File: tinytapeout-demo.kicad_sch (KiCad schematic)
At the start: 137 parts, among them J1 Conn_01x06, J12 613012243121, J13 613012243121, J14 613012243121, J15 USB4500-03-0-A_REVA, J16 2x20_P2.54mm_Pinheader, J17 Conn_01x03, J18 2x20_P2.54mm_Pinheader, J19 Conn_01x02, J2 Conn_01x04, J3 613012243121, J4 TT04_BREAKOUT_REVB, J5 613012243121, J6 613012243121, J7 Conn_01x02, J8 Conn_01x03, J9 Conn_01x24, SW1 434121025816, SW2 434121025816, SW3 434121025816, SW4 418121270808, U1 157112V12700, U2 TLV1117LV33, U3 AP2112K-1.8, U4 74CBTLV3257, U7 W25Q32JVSS, X1 20MHz

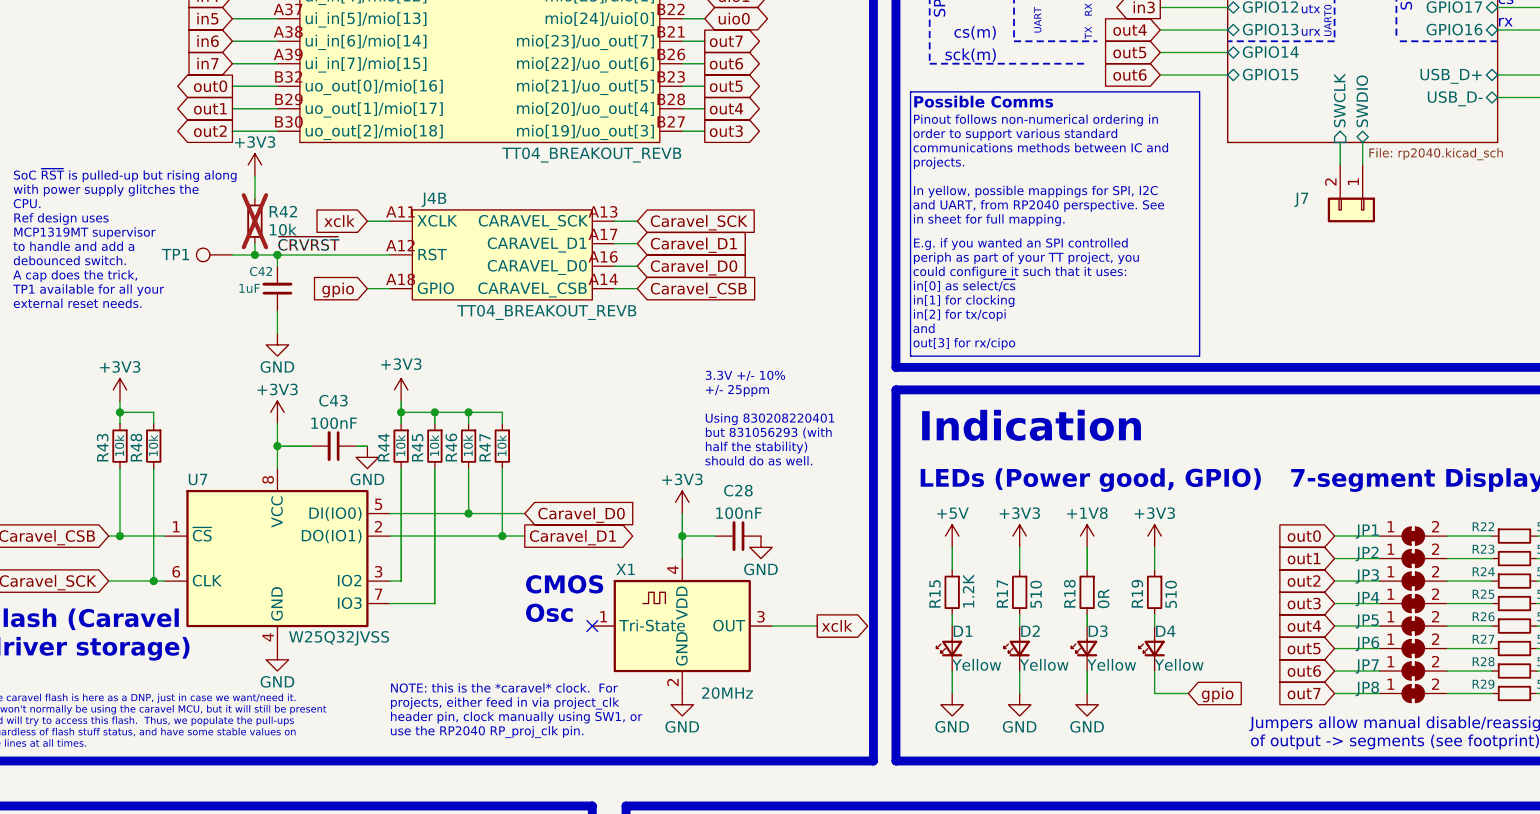
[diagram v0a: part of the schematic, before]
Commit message: Modified silk and BOM for TT04 run
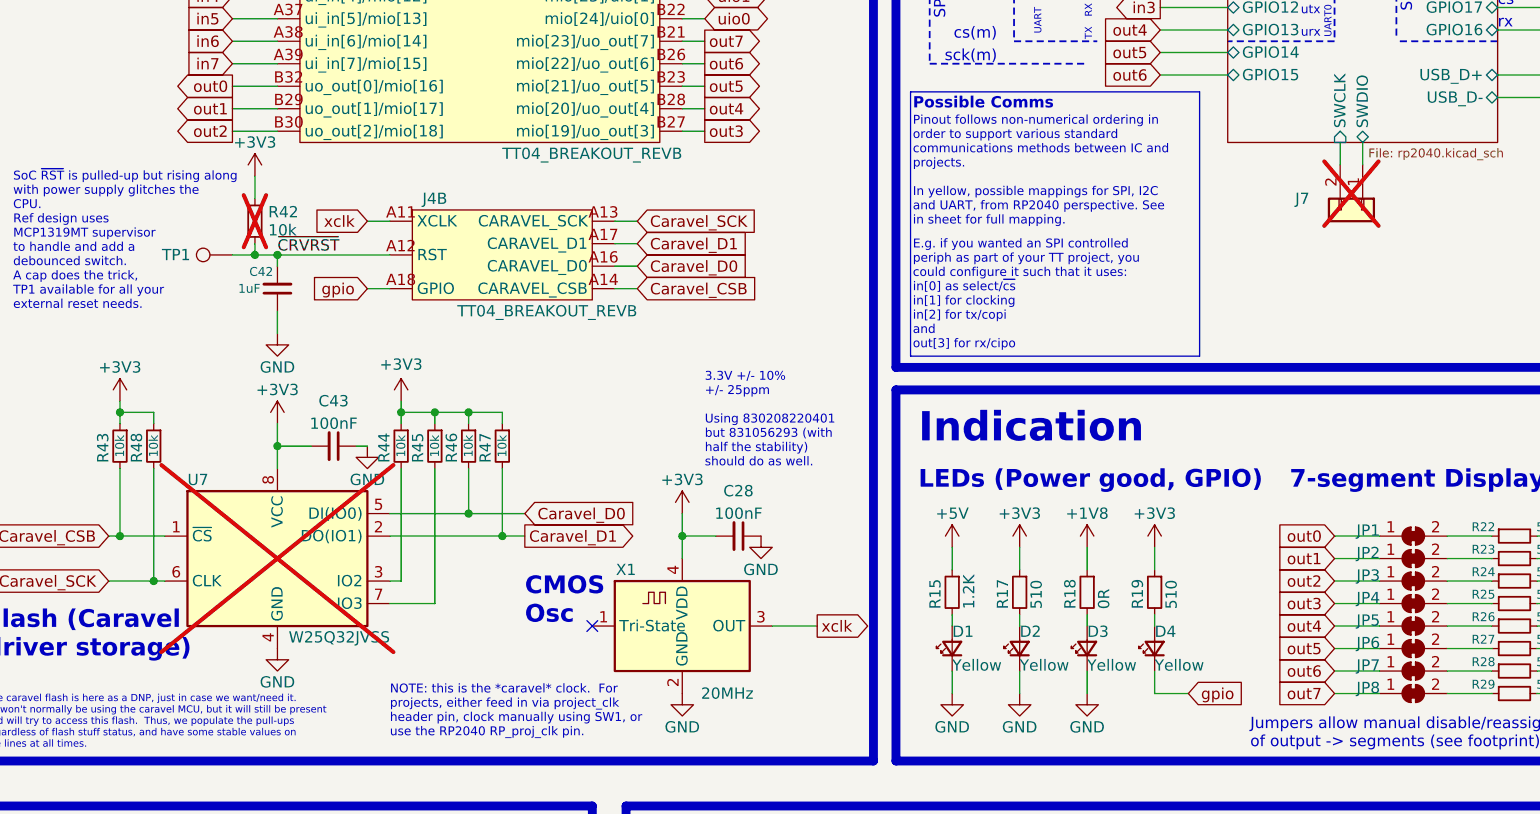
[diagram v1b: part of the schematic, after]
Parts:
- J7, U7: now not fitted
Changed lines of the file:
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@@
 		(title "Tiny Tapeout 4/5 Demo Board")
 		(date "2024-04-12")
-		(rev "1.2.1")
+		(rev "1.2.2")
 		(company "Psychogenic Technologies")
 		(comment 1 "(C) 2023, 2024 Pat Deegan")
@@
 		(in_bom yes)
 		(on_board yes)
-		(dnp no)
+		(dnp yes)
 		(property "Reference" "J7"
 			(at 241.935 165.1 90)
@@
 			)
 		)
+		(property "Variant" ""
+			(at 249.555 166.37 0)
+			(effects
+				(font
+					(size 1.27 1.27)
+				)
+				(hide yes)
+			)
+		)
+		(property "DigikeyPN" ""
+			(at 249.555 166.37 0)
+			(effects
+				(font
+					(size 1.27 1.27)
+				)
+				(hide yes)
+			)
+		)
 		(pin "1"
 		)
@@
 		(in_bom yes)
 		(on_board yes)
-		(dnp no)
+		(dnp yes)
 		(property "Reference" "U7"
 			(at 116.84 196.85 0)

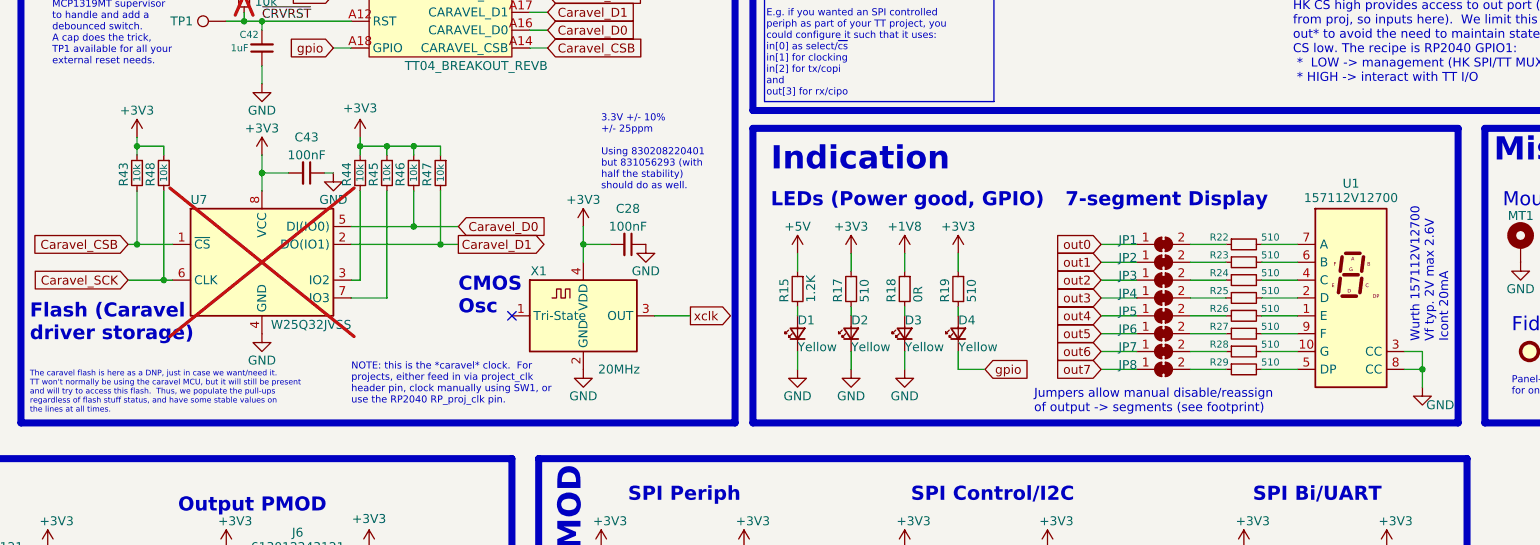
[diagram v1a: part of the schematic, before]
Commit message: v1.2.3, TT05 run plus mod to brighten 1v8 LED (pwr via 3v3, gate fet using 1v8)
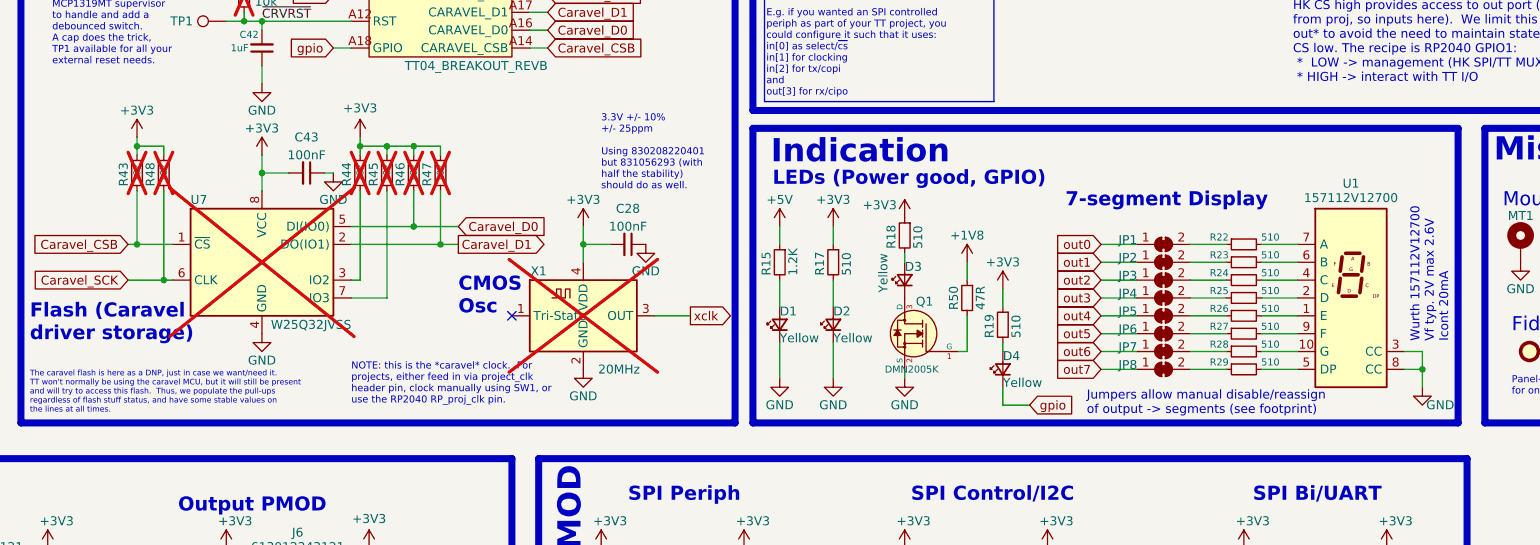
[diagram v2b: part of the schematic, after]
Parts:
- added Q1: DMN2005K, Package_TO_SOT_SMD:SOT-23, symbol psychogenic:DMN2005K
- added R50: 47R, Resistor_SMD:R_0402_1005Metric, symbol Device:R_Small
- R18: value 0R -> 510; footprint Resistor_SMD:R_0603_1608Metric -> Resistor_SMD:R_0402_1005Metric; Characteristics 0R 0603 -> 510R 0402; JLC C95177 -> C276273; MPN RC0603JR-070RL -> RC0402FR-07510RL; MPN_ALT (none) -> CR0402-FX-5100GLF
- R43, R44, R45, R46, R47, R48, X1: now not fitted
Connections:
- net +1V8: now also R50.1; no longer R18.1
- net +3V3: now also R18.1
- net GND: now also Q1.2 (S); no longer D3.1 (K)
- new net: Q1.1 (G), R50.2
- new net: D3.1 (K), Q1.3 (D)
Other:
- moved on the sheet: D1, D2, D3, D4, R15, R17, R18, R19

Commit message: minor tweaks, pre tt06 prep
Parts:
- removed F2: 50mA, Fuse:Fuse_0603_1608Metric, symbol Device:Polyfuse
- J19: footprint Connector_PinHeader_1.27mm:PinHeader_1x02_P1.27mm_Vertical -> Connector_PinHeader_2.54mm:PinHeader_1x02_P2.54mm_Vertical
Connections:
- net 1v8B is gone; now on net +1V8: C13.1, J19.1 (Pin_1), R49.2
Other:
- note added: "50mA hold fuse removed"
- note removed: "50mA hold, 150mA trip in 100ms"
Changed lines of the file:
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@@
 	(wire
 		(pts
-			(xy 246.38 71.12) (xy 247.65 71.12)
-		)
-		(stroke
-			(width 0)
-			(type default)
-		)
-	)
-	(wire
-		(pts
 			(xy 121.92 246.38) (xy 121.92 248.92)
 		)
@@
 	(wire
 		(pts
-			(xy 233.68 83.82) (xy 241.3 83.82)
+			(xy 237.49 83.82) (xy 241.3 83.82)
 		)
 		(stroke
@@
 	(wire
 		(pts
+			(xy 237.49 82.55) (xy 237.49 83.82)
+		)
+		(stroke
+			(width 0)
+			(type default)
+		)
+	)
+	(wire
+		(pts
 			(xy 303.53 68.58) (xy 303.53 66.04)
 		)
@@
 	(wire
 		(pts
-			(xy 231.14 71.12) (xy 238.76 71.12)
+			(xy 231.14 71.12) (xy 247.65 71.12)
 		)
 		(stroke
@@
 	)
 	(image
-		(at 183.515 323.215)
+		(at 183.515 321.945)
 		(data "iVBORw0KGgoAAAANSUhEUgAAAgIAAAC4CAIAAAAe6ROhAAAAA3NCSVQICAjb4U/gAAAgAElEQVR4"
 			"nO3dZ0AURxsA4Hd37w6OztFBekdUBBuIgCKWaDR2o9GoscTeEk3U2Fvsir3H3lHsURFEsYEiKF2Q"
@@
 		)
 	)
-	(text "50mA hold, 150mA \ntrip in 100ms"
+	(text "50mA hold \nfuse removed"
 		(exclude_from_sim no)
-		(at 240.665 78.105 0)
+		(at 242.57 75.692 0)
 		(effects
 			(font
@@
 		)
 	)
-	(label "1v8B"
-		(at 228.6 71.12 0)
-		(fields_autoplaced yes)
-		(effects
-			(font
-				(size 1.27 1.27)
-			)
-			(justify left bottom)
-		)
-	)
-	(label "1v8B"
-		(at 233.68 83.82 0)
-		(fields_autoplaced yes)
-		(effects
-			(font
-				(size 1.27 1.27)
-			)
-			(justify left bottom)
-		)
-	)
 	(label "vfused"
 		(at 143.51 38.1 0)
@@
 			)
 		)
-		(property "Footprint" "Connector_PinHeader_1.27mm:PinHeader_1x02_P1.27mm_Vertical"
+		(property "Footprint" "Connector_PinHeader_2.54mm:PinHeader_1x02_P2.54mm_Vertical"
 			(at 246.38 83.82 0)
 			(effects
@@
 			)
 		)
+		(property "MPN" ""
+			(at 246.38 83.82 0)
+			(effects
+				(font
+					(size 1.27 1.27)
+				)
+				(hide yes)
+			)
+		)
+		(property "MPN_ALT" ""
+			(at 246.38 83.82 0)
+			(effects
+				(font
+					(size 1.27 1.27)
+				)
+				(hide yes)
+			)
+		)
+		(property "DigikeyPN" ""
+			(at 246.38 83.82 0)
+			(effects
+				(font
+					(size 1.27 1.27)
+				)
+				(hide yes)
+			)
+		)
 		(pin "2"
 		)
@@
 	)
 	(symbol
+		(lib_id "power:+1V8")
+		(at 237.49 82.55 0)
+		(unit 1)
+		(exclude_from_sim no)
+		(in_bom yes)
+		(on_board yes)
+		(dnp no)
+		(property "Reference" "#PWR0124"
+			(at 237.49 86.36 0)
+			(effects
+				(font
+					(size 1.27 1.27)
+				)
+				(hide yes)
+			)
+		)
+		(property "Value" "+1V8"
+			(at 237.49 78.74 0)
+			(effects
+				(font
+					(size 1.27 1.27)
+				)
+			)
+		)
+		(property "Footprint" ""
+			(at 237.49 82.55 0)
+			(effects
+				(font
+					(size 1.27 1.27)
+				)
+				(hide yes)
+			)
+		)
+		(property "Datasheet" ""
+			(at 237.49 82.55 0)
+			(effects
+				(font
+					(size 1.27 1.27)
+				)
+				(hide yes)
+			)
+		)
+		(property "Description" ""
+			(at 237.49 82.55 0)
+			(effects
+				(font
+					(size 1.27 1.27)
+				)
+				(hide yes)
+			)
+		)
+		(pin "1"
+		)
+		(instances
+			(project "tinytapeout-demo"
+				(path "/20adca1d-43a1-4784-9682-8b7dd1c7d330"
+					(reference "#PWR0124")
+					(unit 1)
+				)
+			)
+		)
+	)
+	(symbol
 		(lib_id "Device:R_Small")
 		(at 124.46 167.64 0)
@@
 					(unit 1)
 				)
-			)
-		)
-	)
-	(symbol
-		(lib_id "Device:Polyfuse")
-		(at 242.57 71.12 90)
-		(unit 1)
-		(exclude_from_sim no)
-		(in_bom yes)
-		(on_board yes)
-		(dnp no)
-		(property "Reference" "F2"
-			(at 242.57 68.58 90)
-			(effects
-				(font
-					(size 1.27 1.27)
-				)
-			)
-		)
-		(property "Value" "50mA"
-			(at 242.57 73.66 90)
-			(effects
-				(font
-					(size 1.27 1.27)
-				)
-			)
-		)
-		(property "Footprint" "Fuse:Fuse_0603_1608Metric"
-			(at 247.65 69.85 0)
-			(effects
-				(font
-					(size 1.27 1.27)
-				)
-				(justify left)
-				(hide yes)
-			)
-		)
-		(property "Datasheet" "~"
-			(at 242.57 71.12 0)
-			(effects
-				(font
-					(size 1.27 1.27)
-				)
-				(hide yes)
-			)
-		)
-		(property "Description" ""
-			(at 242.57 71.12 0)
-			(effects
-				(font
-					(size 1.27 1.27)
-				)
-				(hide yes)
-			)
-		)
-		(property "MPN" "0ZCM0005FF2G"
-			(at 242.57 71.12 0)
-			(effects
-				(font
-					(size 1.27 1.27)
-				)
-				(hide yes)
-			)
-		)
-		(property "MPN_ALT" "FEMTOSMDC005F-2"
-			(at 242.57 71.12 0)
-			(effects
-				(font
-					(size 1.27 1.27)
-				)
-				(hide yes)
-			)
-		)
-		(property "Characteristics" "PTC Reset Fuse, 50mA Hold, 150mA trip, 0603"
-			(at 242.57 71.12 0)
-			(effects
-				(font
-					(size 1.27 1.27)
-				)
-				(hide yes)
-			)
-		)
-		(property "Variant" ""
-			(at 242.57 71.12 0)
-			(effects
-				(font
-					(size 1.27 1.27)
-				)
-				(hide yes)
-			)
-		)
-		(property "DigikeyPN" ""
-			(at 242.57 71.12 0)
-			(effects
-				(font
-					(size 1.27 1.27)
-				)
-				(hide yes)
-			)
-		)
-		(property "JLC" "C3760470"
-			(at 242.57 71.12 90)
-			(effects
-				(font
-					(size 1.27 1.27)
-				)
-				(hide yes)
-			)
-		)
-		(pin "1"
-		)
-		(pin "2"
-		)
-		(instances
-			(project "tinytapeout-demo"
-				(path "/20adca1d-43a1-4784-9682-8b7dd1c7d330"
-					(reference "F2")
-					(unit 1)
-				)

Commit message: TT06 prelim alpha1 schem
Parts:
- removed C18, C19, C20, C22, C27, C28, C43: 100nF, Capacitor_SMD:C_0402_1005Metric, symbol Device:C_Small
- removed C42: 1uF, Capacitor_SMD:C_0603_1608Metric, symbol Device:C_Small
- removed J4: TT04_BREAKOUT_REVB, TinyTapeout:TT04_BREAKOUT_SMB, symbol TinyTapeout:CARAVEL_TT04_BREAKOUT_REVB
- removed J9: Conn_01x24, Connector_PinHeader_2.54mm:PinHeader_1x24_P2.54mm_Vertical, symbol Connector_Generic:Conn_01x24
- removed NT1: NetTie_2, NetTie:NetTie-2_SMD_Pad0.5mm, symbol Device:NetTie_2
- removed R33: 10k, Resistor_SMD:R_0402_1005Metric, symbol Device:R_Small
- removed TP1: TestPoint, TestPoint:TestPoint_Pad_D1.5mm, symbol Connector:TestPoint
- removed U4: 74CBTLV3257, Package_SO:TSSOP-16_4.4x5mm_P0.65mm, symbol 74xx:74CBTLV3257
- removed U7: W25Q32JVSS, Package_SO:SOIC-8_5.23x5.23mm_P1.27mm, symbol Memory_Flash:W25Q32JVSS
- removed X1: 20MHz, Oscillator:Oscillator_SMD_ECS_2520MV-xxx-xx-4Pin_2.5x2.0mm, symbol Oscillator:ECS-2520MV-xxx-xx
- added J4: TT06_BREAKOUT_REVA, TinyTapeout:TT06_CARRIER_ON_DB, symbol TinyTapeout:OPENFRAME_TT06_BREAKOUT_REVA
- added J9: Conn_01x16, Connector_PinHeader_2.54mm:PinHeader_1x16_P2.54mm_Vertical, symbol Connector_Generic:Conn_01x16
- added R51, R52, R53, R54, R55: 10k, Resistor_SMD:R_0402_1005Metric, symbol Device:R_Small
- R42, R43, R44, R45, R46, R47, R48: now fitted
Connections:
- net Caravel_CSB is gone; now on net GND: R43.2
- net Caravel_D0 is gone; now on net GND: R46.2
- net Caravel_D1 is gone; now on net GND: R47.2
- net Caravel_SCK is gone; now on net GND: R48.2
- net ~{CRVRST} is gone; now on net GND: R42.2
- net +1V8: now also J4.A7 (VCCD), J9.6 (Pin_6)
- net +3V3: now also J4.B2 (VDDA), J4.B4 (VDDIO), J9.4 (Pin_4); no longer R42.1, R43.1, R44.1, R45.1, R46.1, R47.1, R48.1
- net +5V: now also J9.2 (Pin_2)
- net GND: now also R44.2, R45.2, J4.A1 (GND), J4.A12 (GND), J4.A15 (GND), J4.A18 (GND), J4.A21 (GND), J4.A23 (GND), J4.A25 (GND), J4.A27 (GND), J4.A29 (GND), J4.A31 (GND), J4.A32 (GND), J4.A33 (GND), J4.A37 (GND), J4.A38 (GND), J4.A5 (GND), J4.B1 (GND), J4.B10 (GND), J4.B12 (GND), J4.B14 (GND), J4.B16 (GND), J4.B17 (GND), J4.B18 (GND), J4.B23 (GND), J4.B24 (GND), J4.B29 (GND), J4.B3 (GND), J4.B30 (GND), J4.B35 (GND), J4.B36 (GND), J4.B39 (GND), J4.B40 (GND), J4.B6 (GND), J4.B8 (GND), J9.1 (Pin_1), J9.11 (Pin_11), J9.15 (Pin_15), J9.3 (Pin_3), J9.5 (Pin_5), J9.7 (Pin_7), R51.2, R52.2, R53.2, R54.2, R55.2
- net RPIO29: now also J9.16 (Pin_16)
- net ctrl_ena: now also J4.A2 (ctrl_ena), J9.8 (Pin_8)
- net ctrl_sel_inc: now also J4.A3 (ctrl_inc), J9.10 (Pin_10)
- net in0: now also J4.A9 (ui_in[0])
- net in1: now also J4.A11 (ui_in[1])
- net in2: now also J4.A14 (ui_in[2])
- net in3: now also J4.A13 (ui_in[3])
- net in4: now also J4.A17 (ui_in[4])
- net in5: now also J4.A19 (ui_in[5])
- net in6: now also J4.A16 (ui_in[6])
- net in7: now also J4.A34 (ui_in[7])
- net out0: now also J4.B27 (uo_out[0])
- net out1: now also J4.B28 (uo_out[1])
- net out2: now also J4.B25 (uo_out[2])
- net out3: now also J4.B26 (uo_out[3])
- net out4: now also J4.B21 (uo_out[4])
- net out5: now also J4.B22 (uo_out[5])
- net out6: now also J4.B19 (uo_out[6])
- net out7: now also J4.B20 (uo_out[7])
- net project_clk: now also J4.A35 (proj_clk)
- net uio0: now also J4.A39 (uio[0])
- net uio1: now also J4.A40 (uio[1])
- net uio2: now also J4.B37 (uio[2])
- net uio3: now also J4.B38 (uio[3])
- net uio4: now also J4.B33 (uio[4])
- net uio5: now also J4.B34 (uio[5])
- net uio6: now also J4.B31 (uio[6])
- net uio7: now also J4.B32 (uio[7])
- net ~{ctrl_sel_rst}: now also J4.A4 (ctrl_~{rst}), J9.9 (Pin_9)
- net ~{project_rst}: now also J4.A36 (proj_~{rst})
- new net an0: J4.A20 (an0), R47.1
- new net an1: J4.A22 (an1), R46.1
- new net an10: J4.B7 (an10), R54.1
- new net an11: J4.B5 (an11), R55.1
- new net an2: J4.A24 (an2), R45.1
- new net an3: J4.A26 (an3), R44.1
- new net an4: J4.A28 (an4), R43.1
- new net an5: J4.A30 (an5), R42.1
- new net an6: J4.B15 (an6), R48.1
- new net an7: J4.B13 (an7), R51.1
- new net an8: J4.B11 (an8), R52.1
- new net an9: J4.B9 (an9), R53.1
- new net res1: J4.A6 (RES1), J9.12 (Pin_12)
- new net res2: J4.A8 (RES2), J9.13 (Pin_13)
- new net res3: J4.A10 (RES3), J9.14 (Pin_14)
- no-connect marks 4 -> 3
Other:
- note added: "Analog"
- note added: "Analog pins are held low to ensure nice state. Jumpers on carrier may be cut to get rid of the header traversal and termination."
- note added: "Control"
- note added: "I/O"
- note added: "Stronger pull-downs on carrier side allow us to determine if an ASIC board is actually connected (vs and FPGA sim board, or nothing). On startup, read the ctrl en and reset, if they are low, we have an ASIC carrier. From then, drive the lines normally."
- note added: "Tiny Tapeout 06+ Demo Board: PRELIMINARY"
- note removed: ""rx""
- note removed: ""tx""
- note removed: "3.3V +/- 10% +/- 25ppm Using 830208220401 but 831056293 (with half the stability) should do as well."
- note removed: "CMOS Osc"
- note removed: "Extensive labelling, designed for TT4+ with new MUX, RP2040 on board, accessed via USB. Project clock from RP2040, external or manual, DIP switches for inputs, 7-segment display (remappable with jumpers) on outputs, full access to 8 in, out and bidirectionals via PMODs, all pins broken out in headers. Power via +5V USB, or 5V breakout pin. On-board regulation to 3v3 and 1v8. VDDIO is 3v3, includi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"
- note removed: "Flash (Caravel driver storage)"
- note removed: "Misc PU/PD. Project reset is pulled-up via the user switch, project clock PD via its own manual switch."
- note removed: "Multiplexed management/TT outputs"
- note removed: "Multiplexed signals to increase I/O at low cost. HK CS low gives access to both * HK SPI and * TT MUX control HK CS high provides access to out port (read from proj, so inputs here). We limit this to out* to avoid the need to maintain state while CS low. The recipe is RP2040 GPIO1: * LOW -> management (HK SPI/TT MUX) * HIGH -> interact with TT I/O"
- note removed: "NOTE: this is the *caravel* clock. For projects, either feed in via project_clk header pin, clock manually using SW1, or use the RP2040 RP_proj_clk pin."
- note removed: "Net tie used to clarify usage/labelling"
- note removed: "Note: All this decoupling should be amply handled by the carrier. Would rather DNP than regret."
- note removed: "SoC ~{RST} is pulled-up but rising along with power supply glitches the CPU. Ref design uses MCP1319MT supervisor to handle and add a debounced switch. A cap does the trick, TP1 available for all your external reset needs."
- note removed: "TT Mux: ena and ~{RST}, HIGH by default"
- note removed: "The caravel flash is here as a DNP, just in case we want/need it. TT won't normally be using the caravel MCU, but it will still be present and will try to access this flash. Thus, we populate the pull-ups regardless of flash stuff status, and have some stable values on the lines at all times."
- note removed: "Tiny Tapeout 4/5 Demo Board"
- moved on the sheet: C16, C17, C21, C23, C24, C25, C26, D1, D2, D3, D4, FID1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
